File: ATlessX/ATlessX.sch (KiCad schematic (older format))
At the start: 21 parts, among them J1 EXT_PWR_SW, J2 ATX, J3 P8, J4 P9, SW1 Power, U1 74LS74, U2 74LS14, U3 L7905

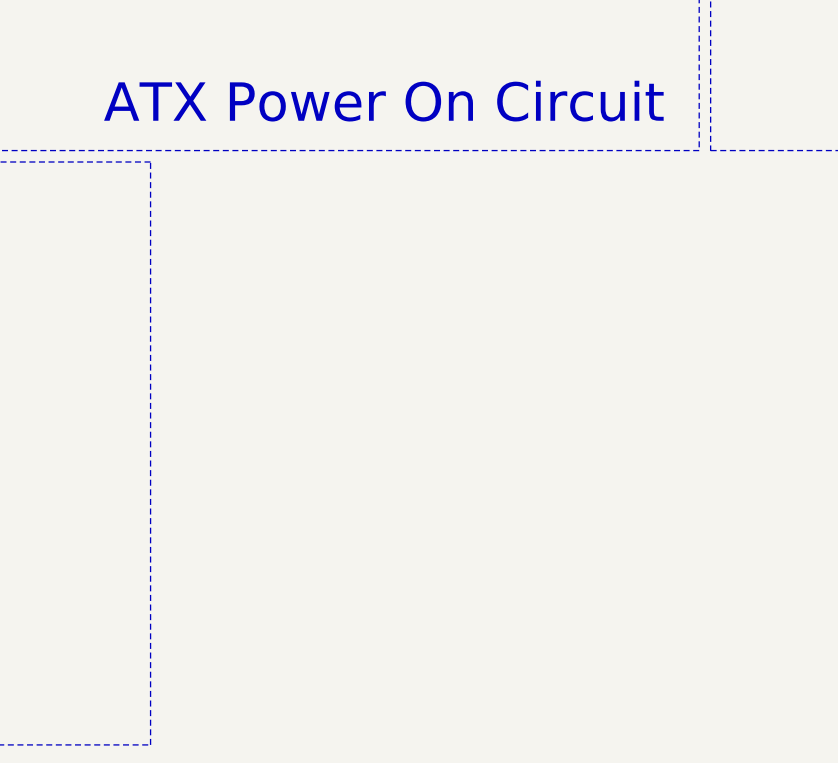
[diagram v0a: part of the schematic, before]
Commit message: Add filter caps
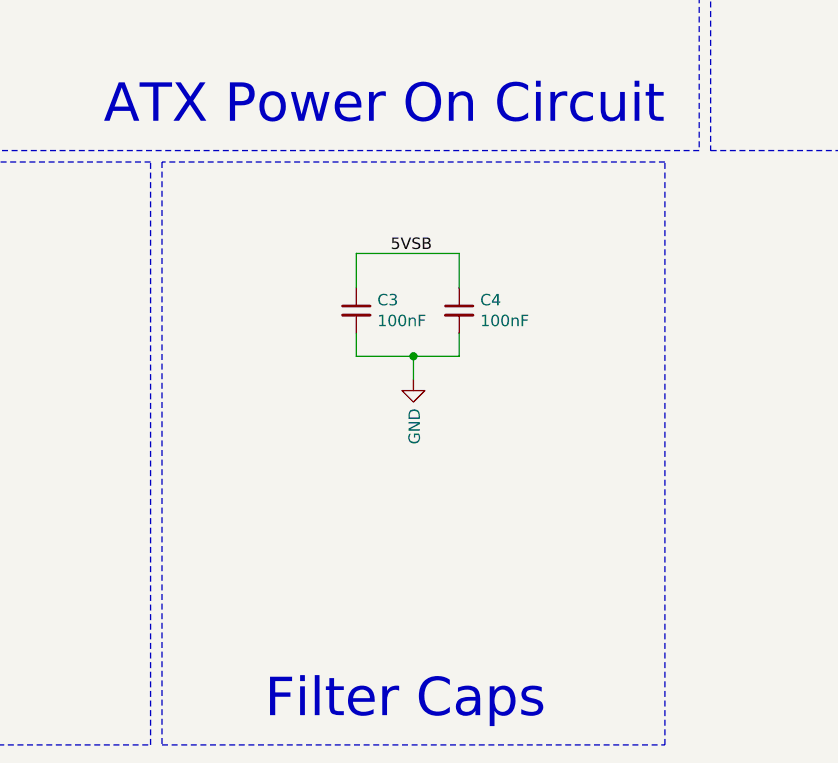
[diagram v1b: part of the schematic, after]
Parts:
- added C3, C4: 100nF, Capacitor_THT:C_Disc_D4.3mm_W1.9mm_P5.00mm, symbol Device:C_Small
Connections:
- net 5VSB: now also C3.1, C4.1
- net GND: now also C3.2, C4.2
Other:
- note added: "Filter Caps"
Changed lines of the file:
@@
 Text Notes 1700 7600 0    168  ~ 0
 AT Connectors
+$Comp
+L Device:C_Small C3
+U 1 1 5DDB0FB5
+P 5450 5800
+F 0 "C3" H 5542 5846 50  0000 L CNN
+F 1 "100nF" H 5542 5755 50  0000 L CNN
+F 2 "Capacitor_THT:C_Disc_D4.3mm_W1.9mm_P5.00mm" H 5450 5800 50  0001 C CNN
+F 3 "~" H 5450 5800 50  0001 C CNN
+	1    5450 5800
+	1    0    0    -1
+$EndComp
+$Comp
+L Device:C_Small C4
+U 1 1 5DDB1122
+P 5900 5800
+F 0 "C4" H 5992 5846 50  0000 L CNN
+F 1 "100nF" H 5992 5755 50  0000 L CNN
+F 2 "Capacitor_THT:C_Disc_D4.3mm_W1.9mm_P5.00mm" H 5900 5800 50  0001 C CNN
+F 3 "~" H 5900 5800 50  0001 C CNN
+	1    5900 5800
+	1    0    0    -1
+$EndComp
+$Comp
+L power:GND #PWR0116
+U 1 1 5DDB5315
+P 5700 6100
+F 0 "#PWR0116" H 5700 5850 50  0001 C CNN
+F 1 "GND" V 5705 5972 50  0000 R CNN
+F 2 "" H 5700 6100 50  0001 C CNN
+F 3 "" H 5700 6100 50  0001 C CNN
+	1    5700 6100
+	1    0    0    -1
+$EndComp
+Wire Wire Line
+	5450 5900 5450 6000
+Wire Wire Line
+	5450 6000 5700 6000
+Wire Wire Line
+	5900 6000 5900 5900
+Wire Wire Line
+	5700 6100 5700 6000
+Connection ~ 5700 6000
+Wire Wire Line
+	5700 6000 5900 6000
+Wire Wire Line
+	5450 5700 5450 5550
+Wire Wire Line
+	5450 5550 5900 5550
+Wire Wire Line
+	5900 5550 5900 5700
+Text Label 5600 5550 0    50   ~ 0
+5VSB
+Wire Notes Line
+	4600 5150 4600 7700
+Wire Notes Line
+	4600 7700 6800 7700
+Wire Notes Line
+	6800 7700 6800 5150
+Wire Notes Line
+	6800 5150 4600 5150
+Text Notes 5050 7600 0    168  ~ 0
+Filter Caps
 $EndSCHEMATC

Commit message: Design PCB
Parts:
- added H1, H2, H3, H4: MountingHole_Pad, MountingHole:MountingHole_3.5mm_Pad, symbol Mechanical:MountingHole_Pad
- added unit 2 of U1
- added unit 4 of U2
- added unit 5 of U2
- added unit 6 of U2
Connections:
- net 5VSB: now also U1.10 (~S)
- net GND: now also H1.1, H2.1, H3.1, H4.1, U1.11 (C), U1.12 (D), U1.13 (~R), U2.11, U2.13, U2.9
- no-connect marks 4 -> 11
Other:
- note added: "Mnt. Holes"
- note added: "Spares"
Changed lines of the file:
@@
 EESchema Schematic File Version 4
-LIBS:ATlessX-cache
-EELAYER 26 0
+EELAYER 30 0
 EELAYER END
 $Descr A4 11693 8268
@@
 Text Notes 5050 7600 0    168  ~ 0
 Filter Caps
+$Comp
+L power:GND #PWR?
+U 1 1 5DDE969D
+P 8150 5900
+F 0 "#PWR?" H 8150 5650 50  0001 C CNN
+F 1 "GND" H 8155 5727 50  0000 C CNN
+F 2 "" H 8150 5900 50  0001 C CNN
+F 3 "" H 8150 5900 50  0001 C CNN
+	1    8150 5900
+	1    0    0    -1
+$EndComp
+$Comp
+L Mechanical:MountingHole_Pad H1
+U 1 1 5DDEF346
+P 7300 5650
+F 0 "H1" H 7200 5653 50  0000 R CNN
+F 1 "MountingHole_Pad" H 7400 5608 50  0001 L CNN
+F 2 "MountingHole:MountingHole_3.5mm_Pad" H 7300 5650 50  0001 C CNN
+F 3 "~" H 7300 5650 50  0001 C CNN
+	1    7300 5650
+	-1   0    0    1
+$EndComp
+$Comp
+L Mechanical:MountingHole_Pad H2
+U 1 1 5DE0ABC9
+P 7700 5650
+F 0 "H2" H 7600 5653 50  0000 R CNN
+F 1 "MountingHole_Pad" H 7800 5608 50  0001 L CNN
+F 2 "MountingHole:MountingHole_3.5mm_Pad" H 7700 5650 50  0001 C CNN
+F 3 "~" H 7700 5650 50  0001 C CNN
+	1    7700 5650
+	-1   0    0    1
+$EndComp
+$Comp
+L Mechanical:MountingHole_Pad H3
+U 1 1 5DE0B090
+P 7300 6050
+F 0 "H3" H 7200 6053 50  0000 R CNN
+F 1 "MountingHole_Pad" H 7400 6008 50  0001 L CNN
+F 2 "MountingHole:MountingHole_3.5mm_Pad" H 7300 6050 50  0001 C CNN
+F 3 "~" H 7300 6050 50  0001 C CNN
+	1    7300 6050
+	-1   0    0    1
+$EndComp
+$Comp
+L Mechanical:MountingHole_Pad H4
+U 1 1 5DE0B551
+P 7700 6050
+F 0 "H4" H 7600 6053 50  0000 R CNN
+F 1 "MountingHole_Pad" H 7800 6008 50  0001 L CNN
+F 2 "MountingHole:MountingHole_3.5mm_Pad" H 7700 6050 50  0001 C CNN
+F 3 "~" H 7700 6050 50  0001 C CNN
+	1    7700 6050
+	-1   0    0    1
+$EndComp
+Wire Wire Line
+	7300 5550 7300 5450
+Wire Wire Line
+	7300 5450 7700 5450
+Wire Wire Line
+	7700 5450 7700 5550
+Wire Wire Line
+	7300 5950 7300 5850
+Wire Wire Line
+	7300 5850 7700 5850
+Wire Wire Line
+	7700 5850 7700 5950
+Wire Wire Line
+	7700 5850 8150 5850
+Wire Wire Line
+	8150 5850 8150 5900
+Connection ~ 7700 5850
+Wire Wire Line
+	7700 5450 8150 5450
+Wire Wire Line
+	8150 5450 8150 5850
+Connection ~ 7700 5450
+Connection ~ 8150 5850
+Wire Notes Line
+	6850 5150 6850 6500
+Wire Notes Line
+	6850 6500 8450 6500
+Wire Notes Line
+	8450 6500 8450 5150
+Wire Notes Line
+	8450 5150 6850 5150
+Text Notes 6950 6450 0    168  ~ 0
+Mnt. Holes
+$Comp
+L 74xx:74LS14 U2
+U 4 1 5DE4CE73
+P 9150 5400
+F 0 "U2" H 9300 5550 50  0000 C CNN
+F 1 "74LS14" H 9550 5550 50  0000 C CNN
+F 2 "" H 9150 5400 50  0001 C CNN
+F 3 "http://www.ti.com/lit/gpn/sn74LS14" H 9150 5400 50  0001 C CNN
+	4    9150 5400
+	1    0    0    -1
+$EndComp
+$Comp
+L 74xx:74LS14 U2
+U 5 1 5DE4E964
+P 9150 5750
+F 0 "U2" H 9300 5900 50  0000 C CNN
+F 1 "74LS14" H 9550 5900 50  0000 C CNN
+F 2 "" H 9150 5750 50  0001 C CNN
+F 3 "http://www.ti.com/lit/gpn/sn74LS14" H 9150 5750 50  0001 C CNN
+	5    9150 5750
+	1    0    0    -1
+$EndComp
+$Comp
+L 74xx:74LS14 U2
+U 6 1 5DE52E83
+P 9150 6100
+F 0 "U2" H 9300 6250 50  0000 C CNN
+F 1 "74LS14" H 9550 6250 50  0000 C CNN
+F 2 "" H 9150 6100 50  0001 C CNN
+F 3 "http://www.ti.com/lit/gpn/sn74LS14" H 9150 6100 50  0001 C CNN
+	6    9150 6100
+	1    0    0    -1
+$EndComp
+$Comp
+L power:GND #PWR?
+U 1 1 5DE66C50
+P 8650 5750
+F 0 "#PWR?" H 8650 5500 50  0001 C CNN
+F 1 "GND" V 8550 5800 50  0000 R CNN
+F 2 "" H 8650 5750 50  0001 C CNN
+F 3 "" H 8650 5750 50  0001 C CNN
+	1    8650 5750
+	0    1    1    0
+$EndComp
+Wire Wire Line
+	8650 5750 8800 5750
+Wire Wire Line
+	8850 5400 8800 5400
+Wire Wire Line
+	8800 5400 8800 5750
+Connection ~ 8800 5750
+Wire Wire Line
+	8800 5750 8850 5750
+Wire Wire Line
+	8800 5750 8800 6100
+Wire Wire Line
+	8800 6100 8850 6100
+Wire Wire Line
+	9450 5400 9600 5400
+Wire Wire Line
+	9450 5750 9600 5750
+Wire Wire Line
+	9450 6100 9600 6100
+NoConn ~ 9600 5400
+NoConn ~ 9600 5750
+NoConn ~ 9600 6100
+NoConn ~ 8100 4500
+$Comp
+L 74xx:74LS74 U1
+U 2 1 5DEAB0BA
+P 10650 5750
+F 0 "U1" H 10650 6228 50  0000 C CNN
+F 1 "74LS74" H 10650 6137 50  0000 C CNN
+F 2 "Package_DIP:DIP-14_W7.62mm_Socket_LongPads" H 10650 5750 50  0001 C CNN
+F 3 "74xx/74hc_hct74.pdf" H 10650 5750 50  0001 C CNN
+	2    10650 5750
+	1    0    0    -1
+$EndComp
+Wire Wire Line
+	10950 5650 11050 5650
+Wire Wire Line
+	10950 5850 11050 5850
+NoConn ~ 11050 5650
+NoConn ~ 11050 5850
+NoConn ~ 8550 4600
+$Comp
+L power:GND #PWR?
+U 1 1 5DECC991
+P 10100 5700
+F 0 "#PWR?" H 10100 5450 50  0001 C CNN
+F 1 "GND" V 10105 5572 50  0000 R CNN
+F 2 "" H 10100 5700 50  0001 C CNN
+F 3 "" H 10100 5700 50  0001 C CNN
+	1    10100 5700
+	0    1    1    0
+$EndComp
+Wire Wire Line
+	10100 5700 10300 5700
+Wire Wire Line
+	10300 5700 10300 5650
+Wire Wire Line
+	10300 5650 10350 5650
+Wire Wire Line
+	10300 5700 10300 5750
+Wire Wire Line
+	10300 5750 10350 5750
+Connection ~ 10300 5700
+Wire Wire Line
+	10300 5750 10300 6100
+Wire Wire Line
+	10300 6100 10650 6100
+Wire Wire Line
+	10650 6100 10650 6050
+Connection ~ 10300 5750
+Wire Wire Line
+	10650 5450 10100 5450
+Text Label 10100 5450 0    50   ~ 0
+5VSB
+Wire Notes Line
+	8500 5150 8500 6500
+Wire Notes Line
+	8500 6500 11150 6500
+Wire Notes Line
+	11150 6500 11150 5150
+Wire Notes Line
+	11150 5150 8500 5150
+Text Notes 9400 6450 0    168  ~ 0
+Spares
 $EndSCHEMATC

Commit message: Fix design, update gerbers
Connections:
- net 12V is gone; now on net +12V: D5.2 (A)
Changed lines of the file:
@@
 5VSB
 Text Label 9900 2150 1    50   ~ 0
-12V
++12V
 Text Label 10000 2150 1    50   ~ 0
 -12V
